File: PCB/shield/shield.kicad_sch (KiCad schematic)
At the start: 20 parts, among them J1 QTR-8A, J13 Conn_01x06, J14 Domino, J15 Domino, J2 QMC5883L, J3 Servo, J4 Domino, J5 Joystick, J6 OLED, J7 L298N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

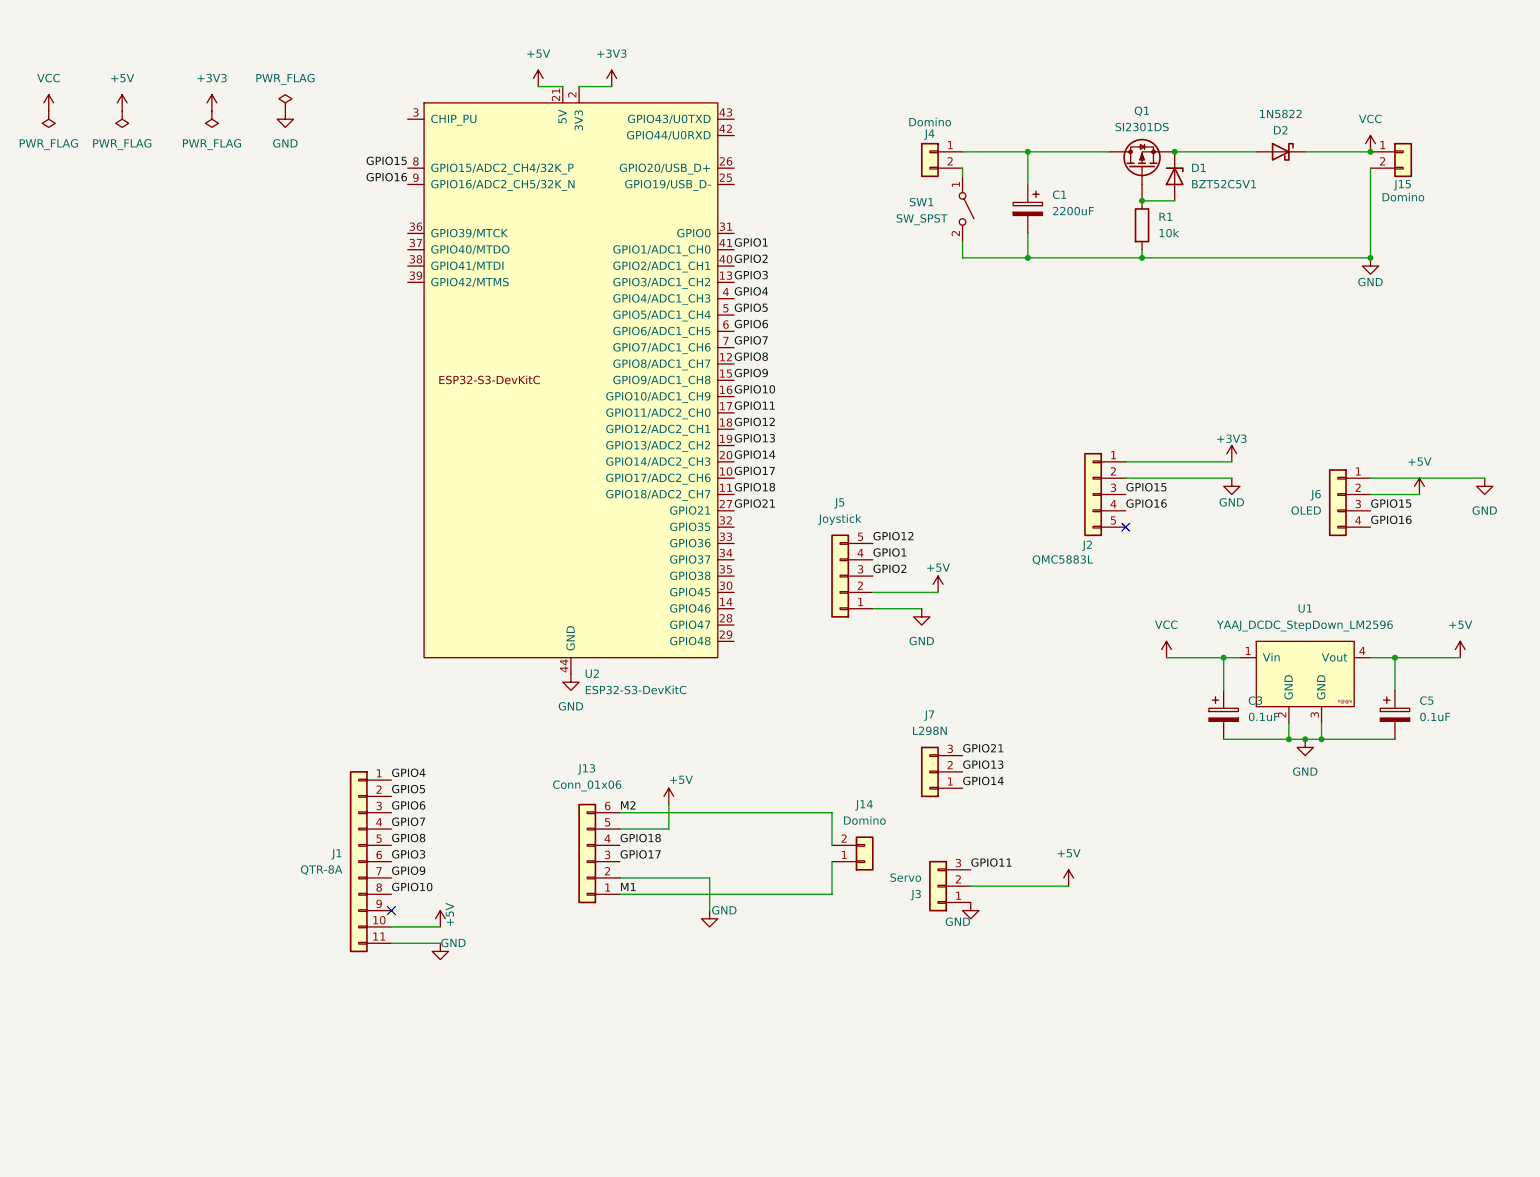
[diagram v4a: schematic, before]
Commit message: feat: change pcb design, use tb6612fng for controlling motor and mosfet for reverse polar protection
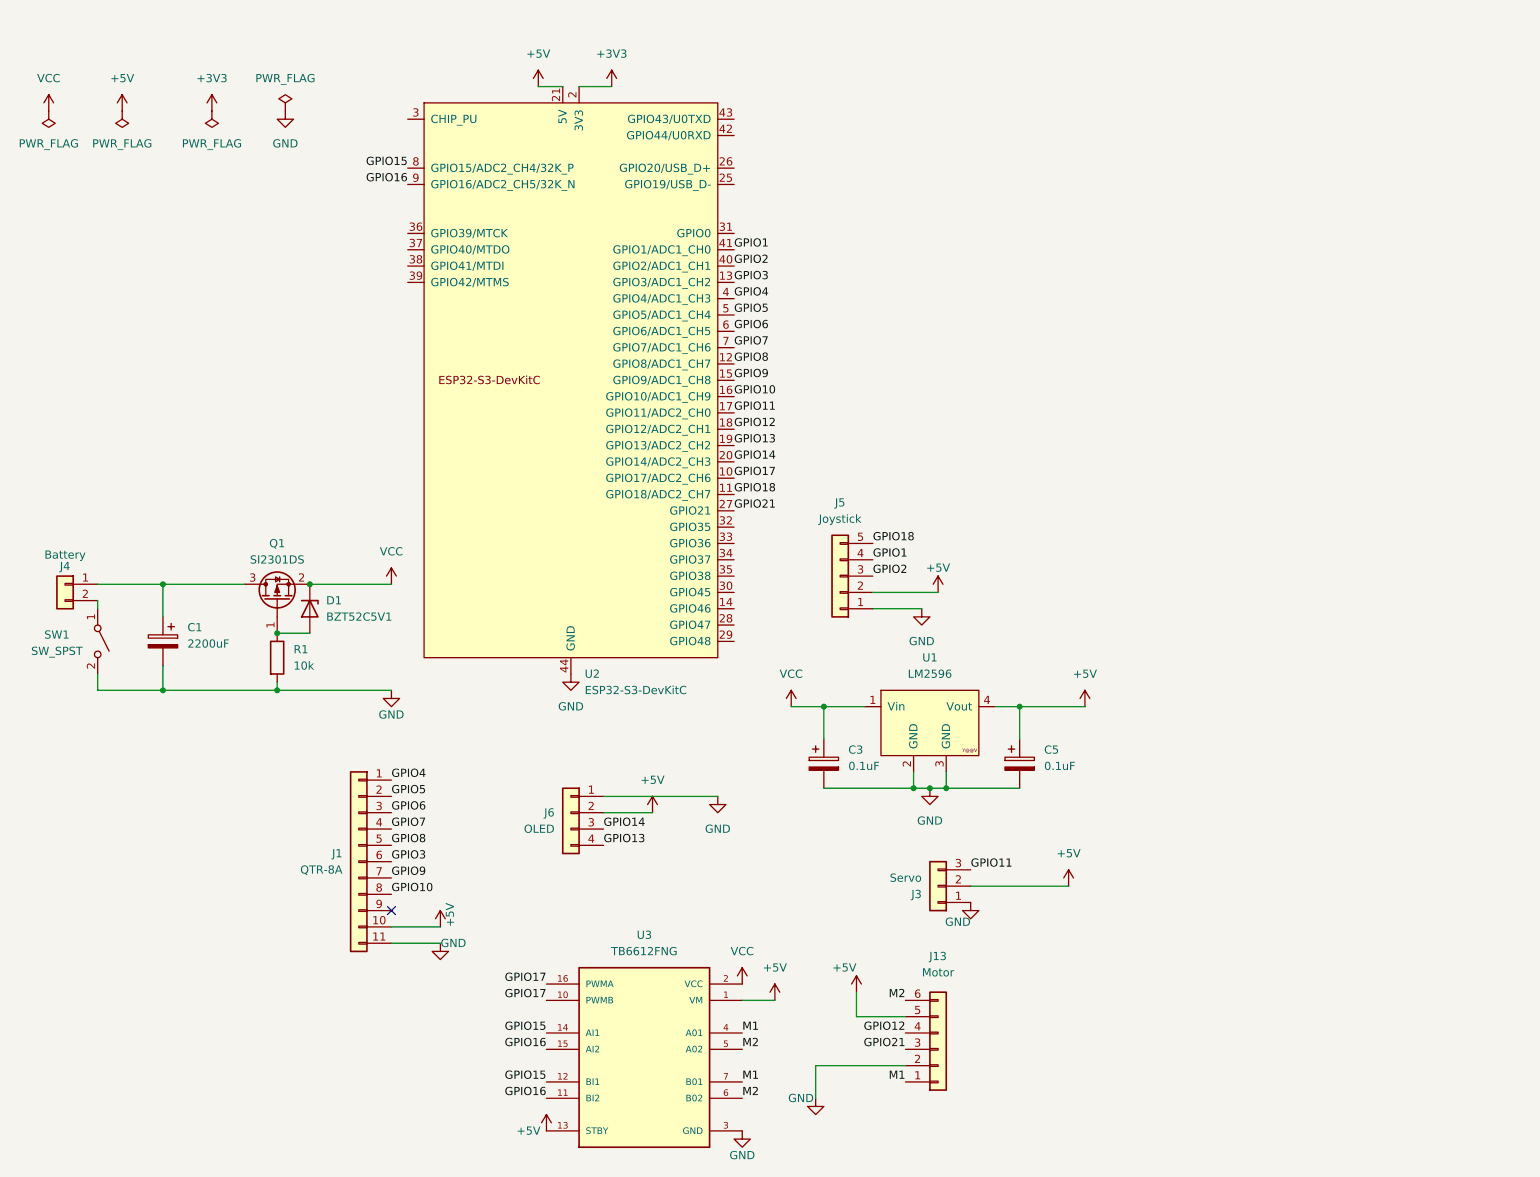
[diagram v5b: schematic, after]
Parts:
- removed D2: 1N5822, Diode_THT:D_DO-201AD_P15.24mm_Horizontal, symbol Diode:1N5822
- removed J14, J15: Domino, TerminalBlock_Phoenix:TerminalBlock_Phoenix_MKDS-1,5-2_1x02_P5.00mm_Horizontal, symbol Connector_Generic:Conn_01x02
- removed J2: QMC5883L, Connector_PinSocket_2.54mm:PinSocket_1x05_P2.54mm_Vertical, symbol Connector_Generic:Conn_01x05
- removed J7: L298N, Connector_JST:JST_XH_B3B-XH-A_1x03_P2.50mm_Vertical, symbol Connector_Generic:Conn_01x03
- removed Q1: SI2301DS, Package_TO_SOT_SMD:SOT-23-3, symbol Device:Q_PMOS
- added Q1: SI2301DS, Package_TO_SOT_SMD:SOT-23-3, symbol Transistor_FET:Q_PMOS_GSD
- added U3: TB6612FNG, TB6612FNG:MODULE_ROB-14450, symbol TB6612FNG:ROB-14450
- C3, C5: footprint Capacitor_THT:CP_Radial_D5.0mm_P2.50mm -> Capacitor_SMD:C_0805_2012Metric_Pad1.18x1.45mm_HandSolder
- J13: value Conn_01x06 -> Motor
- J4: value Domino -> Battery
- SW1: footprint (none) -> Rocket Switch:SW_RF1-1A-DC-2-R-1
- U1: value YAAJ_DCDC_StepDown_LM2596 -> LM2596
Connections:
- net +5V: now also U3.1 (VM), U3.13 (STBY)
- net GND: now also U3.3 (GND), U3.8 (GND), U3.9 (GND)
- net GPIO12: now also J13.4 (Pin_4); no longer J5.5 (Pin_5)
- net GPIO13: now also J6.4 (Pin_4)
- net GPIO14: now also J6.3 (Pin_3)
- net GPIO15: now also U3.12 (BI1), U3.14 (AI1); no longer J6.3 (Pin_3)
- net GPIO16: now also U3.11 (BI2), U3.15 (AI2); no longer J6.4 (Pin_4)
- net GPIO17: now also U3.10 (PWMB), U3.16 (PWMA); no longer J13.3 (Pin_3)
- net GPIO18: now also J5.5 (Pin_5); no longer J13.4 (Pin_4)
- net GPIO21: now also J13.3 (Pin_3)
- net M1: now also U3.4 (A01), U3.7 (B01)
- net M2: now also U3.5 (A02), U3.6 (B02)
- net VCC: now also D1.1 (K), Q1.2 (S), U3.2 (VCC)
- net at D1.2 (A), R1.1: now also Q1.1 (G)
- net at C1.1, J4.1 (Pin_1): now also Q1.3 (D)
- no-connect marks 2 -> 1
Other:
- moved on the sheet: C1, C3, C5, D1, J13, J4, J6, R1, SW1, U1

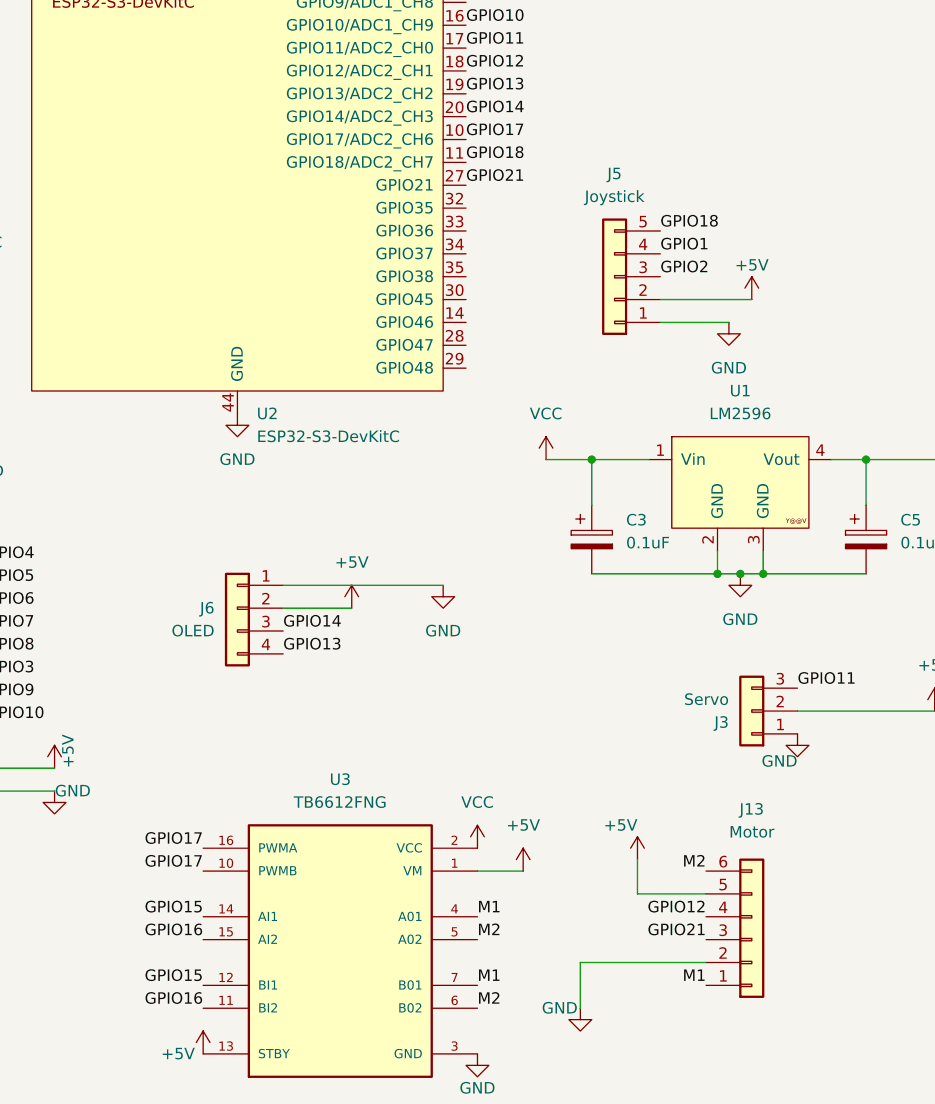
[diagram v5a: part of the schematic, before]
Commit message: feat: change pcb design, make pcb smaller by removing joystick and screen
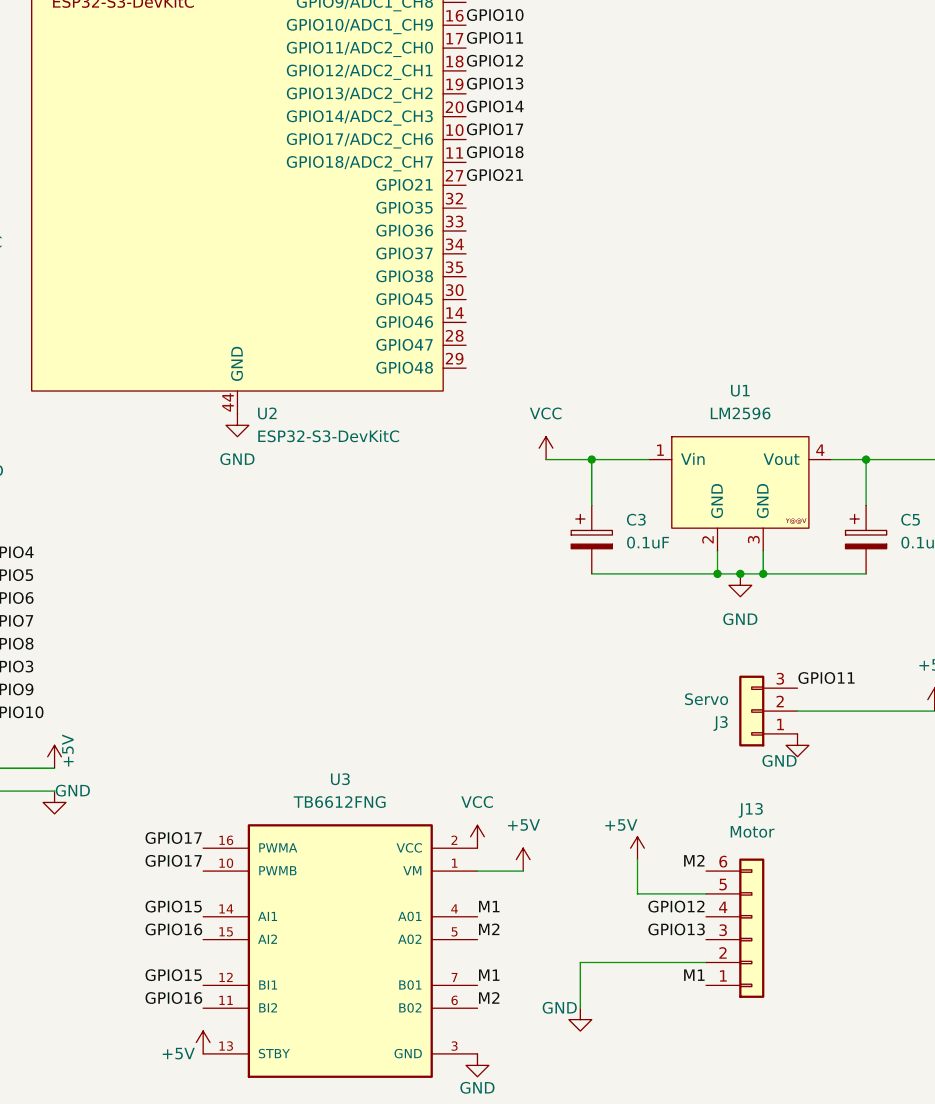
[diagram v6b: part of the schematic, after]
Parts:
- removed J5: Joystick, Connector_PinSocket_2.54mm:PinSocket_1x05_P2.54mm_Vertical, symbol Connector_Generic:Conn_01x05
- removed J6: OLED, Connector_PinSocket_2.54mm:PinSocket_1x04_P2.54mm_Vertical, symbol Connector_Generic:Conn_01x04
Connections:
- net GPIO13: now also J13.3 (Pin_3)
- net GPIO21: no longer J13.3 (Pin_3)
